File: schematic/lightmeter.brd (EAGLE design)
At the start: 27.9 x 52.6 mm, 80 parts, among them IC2 MCP73831/OT, J1 AVR_SPI_PRG_6NS, Q1 NCHANNELMOSFET, Q10 PCHANNELMOSFET, Q11 NCHANNELMOSFET, Q12 NCHANNELMOSFET, Q13 NCHANNELMOSFET, Q14 NCHANNELMOSFET, Q16 NCHANNELMOSFET, Q2 PCHANNELMOSFET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

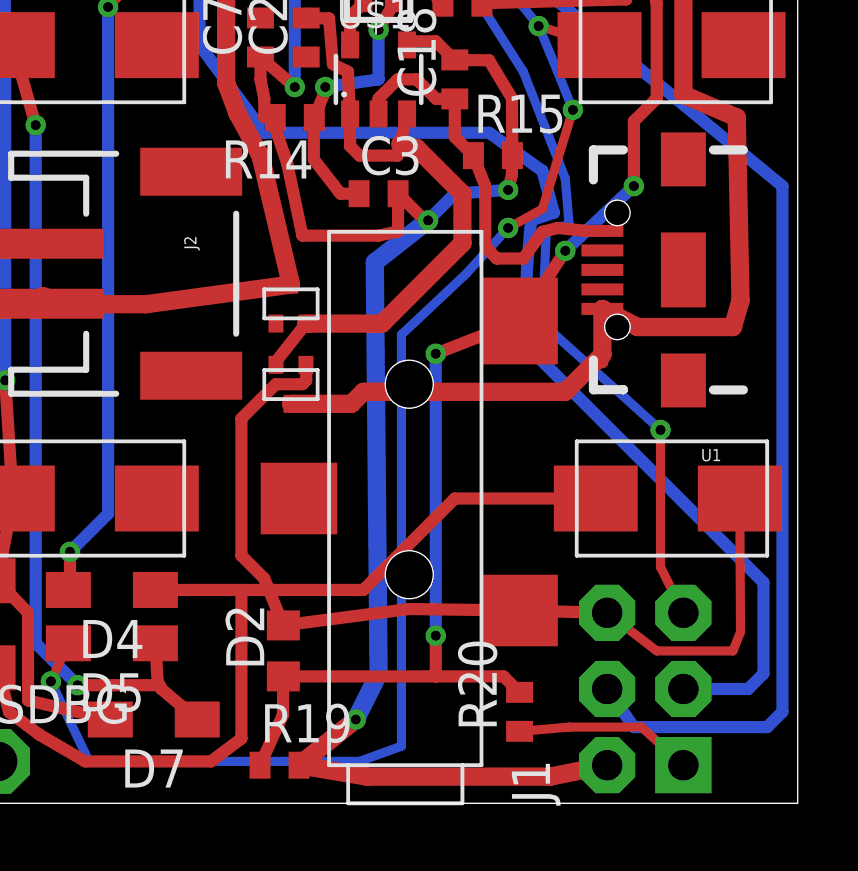
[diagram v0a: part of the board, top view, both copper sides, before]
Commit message: Everything now routed except GND.
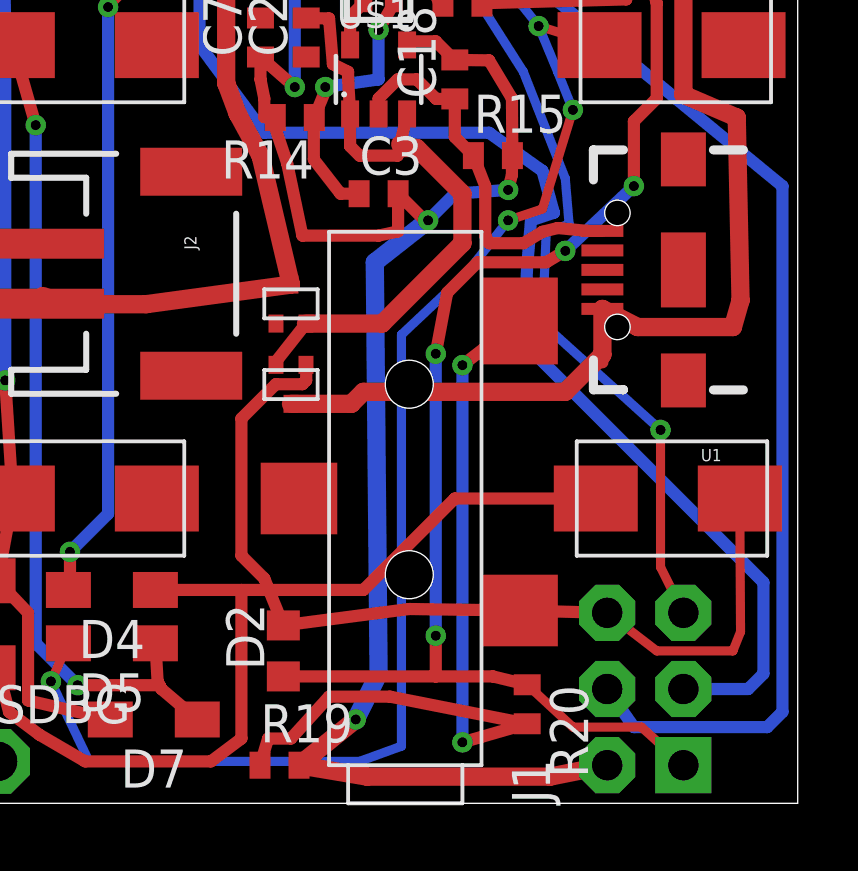
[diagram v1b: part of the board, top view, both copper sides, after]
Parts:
- moved R20 0.36 mm to (17.7, 3.30), turned to 270 degrees
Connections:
- new net N$29: R19.1, R20.2, U$3.P$3
- net AVRMISO/FLASHSYNC: no longer R19.1, R20.2, U$3.P$3
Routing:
- net N$29: track 0.00 -> 27.5 mm, vias 0 -> 2
- net AVRMISO/FLASHSYNC: track 77.3 -> 75.3 mm
- net GND: track 93.4 -> 92.7 mm
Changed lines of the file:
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@@
 <attribute name="SPICEPREFIX" value="R" x="25.4" y="29.845" size="1.778" layer="27" rot="R90" display="off"/>
 </element>
-<element name="R20" library="resistor" package="R0402" value="1K" x="17.399" y="3.048" rot="R90">
-<attribute name="SPICEPREFIX" value="R" x="17.399" y="3.048" size="1.778" layer="27" rot="R90" display="off"/>
+<element name="R20" library="resistor" package="R0402" value="1K" x="17.653" y="3.302" rot="R270">
+<attribute name="SPICEPREFIX" value="R" x="17.653" y="3.302" size="1.778" layer="27" rot="R270" display="off"/>
 </element>
 <element name="R3" library="resistor" package="R0402" value="10k" x="26.035" y="36.068" rot="R90">
@@
 <wire x1="19.655" y1="19.08" x2="18.669" y2="19.177" width="0.4064" layer="1"/>
 <wire x1="18.669" y1="19.177" x2="18.161" y2="19.05" width="0.4064" layer="1"/>
-<wire x1="18.161" y1="19.05" x2="17.526" y2="18.161" width="0.4064" layer="1"/>
-<wire x1="17.526" y1="18.161" x2="16.637" y2="18.161" width="0.4064" layer="1"/>
-<wire x1="16.637" y1="18.161" x2="16.383" y2="18.415" width="0.4064" layer="1"/>
+<wire x1="18.161" y1="19.05" x2="17.526" y2="18.669" width="0.4064" layer="1"/>
+<wire x1="17.526" y1="18.669" x2="16.383" y2="18.669" width="0.4064" layer="1"/>
+<wire x1="16.383" y1="18.669" x2="16.256" y2="18.923" width="0.4064" layer="1"/>
+<wire x1="16.256" y1="18.923" x2="16.256" y2="20.574" width="0.4064" layer="1"/>
+<wire x1="16.256" y1="20.574" x2="15.86" y2="21.59" width="0.4064" layer="1"/>
 <wire x1="22.85" y1="50.857" x2="22.86" y2="49.53" width="0" layer="19" extent="1-16"/>
 <wire x1="18.415" y1="49.53" x2="22.86" y2="49.53" width="0" layer="19" extent="1-1"/>
@@
 <wire x1="25.4" y1="30.495" x2="20.447" y2="29.591" width="0" layer="19" extent="1-1"/>
 <wire x1="26.035" y1="36.718" x2="25.4" y2="30.495" width="0" layer="19" extent="1-1"/>
-<wire x1="10.279" y1="14.616" x2="16.637" y2="18.161" width="0" layer="19" extent="1-1"/>
+<wire x1="10.279" y1="14.616" x2="16.256" y2="18.923" width="0" layer="19" extent="1-1"/>
 <wire x1="9.279" y1="15.991" x2="10.279" y2="14.616" width="0" layer="19" extent="1-1"/>
 <wire x1="5.307990625" y1="10.16" x2="8.128" y2="8.255" width="0" layer="19" extent="1-1"/>
 <wire x1="1.253" y1="18.653" x2="5.307990625" y2="25.273" width="0" layer="19" extent="1-1"/>
-<wire x1="16.383" y1="18.415" x2="16.256" y2="18.669" width="0.4064" layer="1"/>
-<wire x1="16.256" y1="18.669" x2="16.256" y2="20.574" width="0.4064" layer="1"/>
-<wire x1="16.256" y1="20.574" x2="15.86" y2="21.59" width="0.4064" layer="1"/>
 </signal>
 <signal name="VCC">
@@
 <contactref element="IC$3" pad="17"/>
 <contactref element="J1" pad="1"/>
-<contactref element="U$3" pad="P$3"/>
-<contactref element="R19" pad="1"/>
-<contactref element="R20" pad="2"/>
 <contactref element="R20" pad="1"/>
 <contactref element="D2" pad="1"/>
-<wire x1="8.748" y1="1.27" x2="9.51" y2="2.945" width="0.4064" layer="1"/>
-<wire x1="9.51" y1="2.945" x2="9.525" y2="4.23" width="0.4064" layer="1"/>
 <wire x1="9.525" y1="4.23" x2="14.605" y2="4.23" width="0.4064" layer="1"/>
-<wire x1="14.605" y1="4.23" x2="16.867" y2="4.23" width="0.4064" layer="1"/>
-<wire x1="16.867" y1="4.23" x2="17.399" y2="3.698" width="0.4064" layer="1"/>
+<wire x1="14.605" y1="4.23" x2="16.51" y2="4.23" width="0.4064" layer="1"/>
 <wire x1="4.94538125" y1="42.128" x2="4.953" y2="43.561" width="0.254" layer="1"/>
 <wire x1="4.953" y1="43.561" x2="5.588" y2="44.196" width="0.254" layer="1"/>
@@
 <wire x1="14.097" y1="34.417" x2="14.224" y2="33.147" width="0.4064" layer="16"/>
 <via x="18.923" y="18.415" extent="1-16" drill="0.3302" shape="square"/>
-<wire x1="18.923" y1="18.415" x2="17.399" y2="16.0782" width="0.4064" layer="1"/>
 <via x="18.161" y="32.893" extent="1-16" drill="0.3302" shape="square"/>
 <wire x1="18.161" y1="32.893" x2="18.923" y2="32.258" width="0.4064" layer="1"/>
@@
 <via x="21.209" y="20.574" extent="1-16" drill="0.3302" shape="square"/>
 <wire x1="21.209" y1="20.574" x2="18.923" y2="18.415" width="0.4064" layer="16"/>
-<wire x1="17.399" y1="16.0782" x2="14.605" y2="14.986" width="0.4064" layer="1"/>
 <via x="14.605" y="14.986" extent="1-16" drill="0.3302" shape="square"/>
 <wire x1="14.605" y1="14.986" x2="14.605" y2="5.588" width="0.4064" layer="16"/>
 <via x="14.605" y="5.588" extent="1-16" drill="0.3302" shape="square"/>
 <wire x1="14.605" y1="5.588" x2="14.605" y2="4.23" width="0.4064" layer="1"/>
-<wire x1="17.399" y1="2.398" x2="19.05" y2="2.54" width="0.3048" layer="1"/>
-<wire x1="19.05" y1="2.54" x2="21.463" y2="2.54" width="0.3048" layer="1"/>
+<wire x1="17.653" y1="3.952" x2="19.177" y2="2.54" width="0.3048" layer="1"/>
+<wire x1="19.177" y1="2.54" x2="21.463" y2="2.54" width="0.3048" layer="1"/>
 <wire x1="21.463" y1="2.54" x2="22.86" y2="1.27" width="0.3048" layer="1"/>
 <wire x1="21.209" y1="20.574" x2="21.209" y2="22.733" width="0.4064" layer="1"/>
@@
 <wire x1="18.161" y1="32.893" x2="15.748" y2="33.401" width="0.4064" layer="16"/>
 <wire x1="15.748" y1="33.401" x2="14.224" y2="33.147" width="0.4064" layer="16"/>
-<wire x1="17.399" y1="3.698" x2="17.399" y2="2.398" width="0" layer="19" extent="1-1"/>
+<wire x1="16.51" y1="4.23" x2="17.653" y2="3.952" width="0.4064" layer="1"/>
+<wire x1="16.002" y1="18.034" x2="18.288" y2="18.034" width="0.4064" layer="1"/>
+<wire x1="18.288" y1="18.034" x2="18.923" y2="18.415" width="0.4064" layer="1"/>
+<wire x1="14.605" y1="14.986" x2="14.986" y2="17.018" width="0.4064" layer="1"/>
+<wire x1="14.986" y1="17.018" x2="16.002" y2="18.034" width="0.4064" layer="1"/>
 </signal>
 <signal name="OAOUT1">
@@
 <wire x1="18.669" y1="24.384" x2="19.177" y2="23.114" width="0.3048" layer="16"/>
 <via x="19.177" y="23.114" extent="1-16" drill="0.3302" shape="square"/>
-<via x="17.018" y="19.177" extent="1-16" drill="0.3302" shape="square"/>
-<wire x1="17.018" y1="19.177" x2="15.621" y2="17.653" width="0.3048" layer="16"/>
+<via x="17.018" y="19.431" extent="1-16" drill="0.3302" shape="square"/>
+<wire x1="17.018" y1="19.431" x2="15.621" y2="17.653" width="0.3048" layer="16"/>
 <wire x1="15.621" y1="17.653" x2="13.462" y2="15.621" width="0.3048" layer="16"/>
 <wire x1="13.462" y1="15.621" x2="13.462" y2="1.905" width="0.3048" layer="16"/>
@@
 <via x="1.778" y="4.064" extent="1-16" drill="0.3302" shape="square"/>
 <wire x1="1.778" y1="4.064" x2="2.36" y2="5.334" width="0.3048" layer="1"/>
-<wire x1="17.018" y1="19.177" x2="18.161" y2="19.812" width="0.3048" layer="1"/>
+<wire x1="17.018" y1="19.431" x2="18.161" y2="19.812" width="0.3048" layer="1"/>
 <wire x1="18.161" y1="19.812" x2="19.177" y2="23.114" width="0.3048" layer="1"/>
 </signal>
@@
 <wire x1="5.461" y1="29.464" x2="6.358" y2="29.475" width="0.6096" layer="1"/>
 </signal>
+<signal name="N$29">
+<contactref element="R20" pad="2"/>
+<contactref element="U$3" pad="P$3"/>
+<contactref element="R19" pad="1"/>
+<wire x1="17.653" y1="2.652" x2="13.081" y2="3.556" width="0.4064" layer="1"/>
+<wire x1="13.081" y1="3.556" x2="11.049" y2="3.556" width="0.4064" layer="1"/>
+<wire x1="11.049" y1="3.556" x2="9.779" y2="2.159" width="0.4064" layer="1"/>
+<wire x1="9.779" y1="2.159" x2="9.017" y2="2.159" width="0.4064" layer="1"/>
+<wire x1="9.017" y1="2.159" x2="8.748" y2="1.27" width="0.4064" layer="1"/>
+<wire x1="17.399" y1="16.0782" x2="15.494" y2="14.605" width="0.4064" layer="1"/>
+<via x="15.494" y="14.605" extent="1-16" drill="0.3302" shape="square"/>
+<wire x1="15.494" y1="14.605" x2="15.494" y2="2.032" width="0.4064" layer="16"/>
+<via x="15.494" y="2.032" extent="1-16" drill="0.3302" shape="square"/>
+<wire x1="15.494" y1="2.032" x2="17.653" y2="2.652" width="0.4064" layer="1"/>
+</signal>
 </signals>

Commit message: Work on clearences.
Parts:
- moved J2 0.40 mm to (5.08, 17.3)
- moved Q8 0.13 mm to (0.64, 43.1)
- moved R22 0.07 mm to (0.30, 36.9)
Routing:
- net GND: track 92.7 -> 83.3 mm
- net AVRMOSI/BATVOLTAGE: track 29.1 -> 27.2 mm
- net DIODESW$1: track 27.4 -> 29.0 mm
- net AVRSCK: track 54.3 -> 53.7 mm

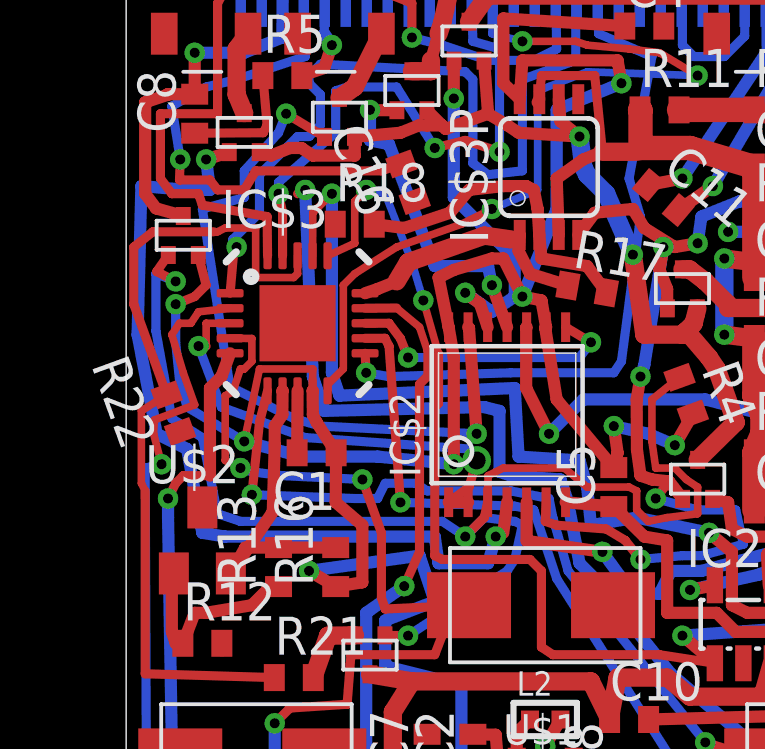
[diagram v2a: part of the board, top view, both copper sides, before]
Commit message: Some more work on clearences.
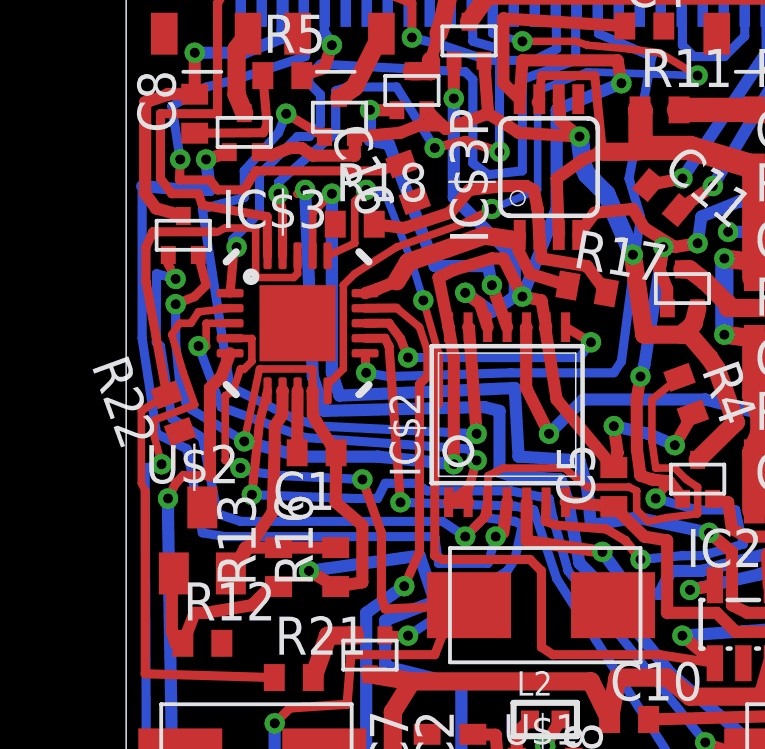
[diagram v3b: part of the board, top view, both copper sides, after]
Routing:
- net SCRPWR: track 44.2 -> 43.6 mm
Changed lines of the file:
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@@
 <wire x1="9.48" y1="33.9122" x2="10.16" y2="34.417" width="0.3048" layer="1"/>
 <wire x1="10.16" y1="34.417" x2="10.414" y2="35.306" width="0.3048" layer="1"/>
-<via x="10.414" y="35.306" extent="1-16" drill="0.6" shape="square"/>
+<via x="10.414" y="35.306" extent="1-16" drill="0.3302" shape="square"/>
 <wire x1="10.414" y1="35.306" x2="10.16" y2="35.687" width="0.3048" layer="16"/>
 <wire x1="10.16" y1="35.687" x2="4.699" y2="36.068" width="0.3048" layer="16"/>
@@
 <wire x1="10.033" y1="32.766" x2="9.271" y2="33.274" width="0.3048" layer="16"/>
 <wire x1="9.271" y1="33.274" x2="2.54" y2="33.274" width="0.3048" layer="16"/>
-<via x="0.381" y="41.275" extent="1-16" drill="0.3302" shape="square"/>
-<wire x1="0.381" y1="41.275" x2="-0.251434375" y2="41.59968125" width="0.3048" layer="1"/>
+<via x="0.381" y="41.35628125" extent="1-16" drill="0.3302" shape="square"/>
+<wire x1="0.381" y1="41.35628125" x2="0.129565625" y2="41.85368125" width="0.3048" layer="1"/>
 <contactref element="Q16" pad="P$1"/>
 <wire x1="7.358" y1="29.475" x2="8.128" y2="29.464" width="0.3048" layer="1"/>
@@
 <wire x1="11.684" y1="33.274" x2="10.668" y2="33.401" width="0.3048" layer="16"/>
 <wire x1="10.668" y1="33.401" x2="10.033" y2="32.766" width="0.3048" layer="16"/>
-<wire x1="-0.251434375" y1="41.59968125" x2="0.135" y2="42.153" width="0.3048" layer="1"/>
-<wire x1="-0.2794" y1="39.624" x2="-0.2794" y2="41.529" width="0.3048" layer="16"/>
-<wire x1="-0.2794" y1="41.529" x2="0.381" y2="41.275" width="0.3048" layer="16"/>
+<wire x1="0.129565625" y1="41.85368125" x2="0.135" y2="42.153" width="0.3048" layer="1"/>
+<wire x1="-0.2667" y1="39.243" x2="-0.256540625" y2="41.529" width="0.3048" layer="16"/>
+<wire x1="-0.256540625" y1="41.529" x2="0.381" y2="41.35628125" width="0.3048" layer="16"/>
 <wire x1="17.176684375" y1="38.0758" x2="16.256" y2="37.338" width="0.254" layer="1"/>
 <wire x1="16.256" y1="37.338" x2="16.256" y2="35.941" width="0.254" layer="1"/>
@@
 <wire x1="17.018" y1="35.052" x2="16.383" y2="35.052" width="0.254" layer="1"/>
 <wire x1="16.383" y1="35.052" x2="16.256" y2="35.941" width="0.254" layer="1"/>
-<wire x1="-0.2794" y1="39.624" x2="0.254" y2="36.703" width="0.3048" layer="16"/>
 <wire x1="0.254" y1="36.703" x2="1.27" y2="36.068" width="0.3048" layer="16"/>
 <wire x1="1.27" y1="36.068" x2="1.778" y2="33.528" width="0.3048" layer="16"/>
 <wire x1="1.778" y1="33.528" x2="2.54" y2="33.274" width="0.3048" layer="16"/>
+<wire x1="-0.2667" y1="39.243" x2="-0.127" y2="39.116" width="0.3048" layer="16"/>
+<wire x1="-0.127" y1="39.116" x2="0.254" y2="36.703" width="0.3048" layer="16"/>
 </signal>
 <signal name="AVRRST">
@@
 <wire x1="2.167" y1="45.582" x2="1.397" y2="45.339" width="0.4064" layer="1"/>
 <via x="1.397" y="45.339" extent="1-16" drill="0.3302" shape="square"/>
-<wire x1="-0.762" y1="44.45" x2="-0.889" y2="39.497" width="0.4064" layer="16"/>
+<wire x1="-0.7366" y1="44.45" x2="-0.7366" y2="39.37" width="0.3048" layer="16"/>
 <via x="11.049" y="32.766" extent="1-16" drill="0.3302" shape="square"/>
 <wire x1="11.43" y1="33.9122" x2="11.303" y2="32.893" width="0.4064" layer="1"/>
 <wire x1="11.303" y1="32.893" x2="11.049" y2="32.766" width="0.3048" layer="1"/>
-<wire x1="11.049" y1="32.766" x2="10.795" y2="31.877" width="0.4064" layer="16"/>
-<wire x1="10.795" y1="31.877" x2="9.144" y2="31.877" width="0.4064" layer="16"/>
-<wire x1="9.144" y1="31.877" x2="9.017" y2="32.766" width="0.4064" layer="16"/>
-<wire x1="9.017" y1="32.766" x2="2.032" y2="32.766" width="0.4064" layer="16"/>
-<wire x1="-0.762" y1="44.45" x2="0.762" y2="44.323" width="0.4064" layer="16"/>
+<wire x1="11.049" y1="32.766" x2="10.795" y2="31.877" width="0.3048" layer="16"/>
+<wire x1="10.795" y1="31.877" x2="9.144" y2="31.877" width="0.3048" layer="16"/>
+<wire x1="9.144" y1="31.877" x2="9.017" y2="32.766" width="0.3048" layer="16"/>
+<wire x1="9.017" y1="32.766" x2="2.032" y2="32.766" width="0.3048" layer="16"/>
+<wire x1="-0.7366" y1="44.45" x2="0.762" y2="44.323" width="0.4064" layer="16"/>
 <wire x1="0.762" y1="44.323" x2="1.524" y2="44.323" width="0.4064" layer="16"/>
 <wire x1="1.524" y1="44.323" x2="1.397" y2="45.339" width="0.4064" layer="16"/>
-<wire x1="-0.889" y1="39.497" x2="-0.254" y2="36.195" width="0.4064" layer="16"/>
-<wire x1="-0.254" y1="36.195" x2="0.762" y2="35.687" width="0.4064" layer="16"/>
-<wire x1="0.762" y1="35.687" x2="1.27" y2="32.893" width="0.4064" layer="16"/>
-<wire x1="1.27" y1="32.893" x2="2.032" y2="32.766" width="0.4064" layer="16"/>
+<wire x1="-0.7366" y1="39.37" x2="-0.254" y2="36.195" width="0.3048" layer="16"/>
+<wire x1="-0.254" y1="36.195" x2="0.762" y2="35.687" width="0.3048" layer="16"/>
+<wire x1="0.762" y1="35.687" x2="1.27" y2="32.893" width="0.3048" layer="16"/>
+<wire x1="1.27" y1="32.893" x2="2.032" y2="32.766" width="0.3048" layer="16"/>
 </signal>
 <signal name="DIODESW$4">
@@
 <contactref element="R21" pad="1"/>
 <contactref element="R22" pad="2"/>
-<wire x1="0.082484375" y1="37.4916" x2="-1.016" y2="40.513" width="0.3048" layer="1"/>
-<wire x1="-1.016" y1="40.513" x2="-1.016" y2="42.418" width="0.3048" layer="1"/>
-<wire x1="-1.016" y1="42.418" x2="-0.381" y2="42.926" width="0.3048" layer="1"/>
+<wire x1="0.082484375" y1="37.4916" x2="-0.6096" y2="41.275" width="0.3048" layer="1"/>
+<wire x1="-0.6096" y1="41.275" x2="-0.6096" y2="42.418" width="0.3048" layer="1"/>
+<wire x1="-0.6096" y1="42.418" x2="-0.381" y2="42.926" width="0.3048" layer="1"/>
 <wire x1="-0.381" y1="42.926" x2="1.651" y2="42.926" width="0.3048" layer="1"/>
 <wire x1="1.651" y1="42.926" x2="1.778" y2="42.926" width="0.254" layer="1"/>

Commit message: More work on clearences.
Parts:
- moved C1 0.40 mm to (5.46, 35.7)
- turned R17 to 0 degrees
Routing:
- net PBI$3: track 67.3 -> 69.3 mm
- net N$8: track 30.9 -> 32.6 mm, vias 0 -> 2
- net VUSB: track 41.0 -> 42.5 mm
- net N$29: track 27.5 -> 28.6 mm
- net DIODESW$3: track 12.2 -> 13.3 mm
- net VREG: track 141.8 -> 142.8 mm
- net N$7: track 27.9 -> 28.6 mm
- net SCRPWR: track 43.6 -> 44.2 mm

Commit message: More work on layout.
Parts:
- moved R4 0.41 mm to (17.6, 37.1)
- moved TSDBG 0.28 mm to (0.25, 1.52)
- moved Q7 0.13 mm to (25.5, 44.6)
- moved R1 0.08 mm to (22.4, 29.8)
- moved C5 0.05 mm to (14.9, 34.4)
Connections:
- net OAPWR: now also Q7.P$1
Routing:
- net GND: track 83.3 -> 69.1 mm, vias 2 -> 0
- net OAPWR: track 20.4 -> 29.6 mm, vias 2 -> 3
- net STG$2: track 23.9 -> 20.2 mm
- net N$8: track 32.6 -> 35.3 mm
- net N$26: track 30.6 -> 32.1 mm
- net N$6: track 14.7 -> 14.0 mm
- net PBI$2: track 40.0 -> 39.3 mm
- net AVRMISO/FLASHSYNC: track 75.3 -> 75.8 mm

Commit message: More work on layout.
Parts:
- moved C4 0.07 mm to (16.0, 49.9)
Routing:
- net DIODESW$3: track 13.3 -> 13.9 mm

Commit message: More work on layout.
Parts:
- moved Q14 0.25 mm to (8.26, 47.6)
- moved Q12 0.13 mm to (5.84, 46.9)
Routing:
- net SCRDAT: track 19.4 -> 27.5 mm
- net SCRCS: track 22.9 -> 24.3 mm
- net SCRCLK: track 28.3 -> 28.4 mm, vias 3 -> 4
